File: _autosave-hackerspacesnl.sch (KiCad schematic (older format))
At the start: 55 parts, among them J1 Screw_Terminal_01x02, J2 Conn_01x04_Male, Q1 Q_NMOS_GSD, Q2 Q_NMOS_GSD, Q3 Q_NMOS_GSD, Q4 Q_NMOS_GSD, Q5 Q_NMOS_GSD, Q6 Q_NMOS_GSD, SW1 SW_Push, SW2 SW_Push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

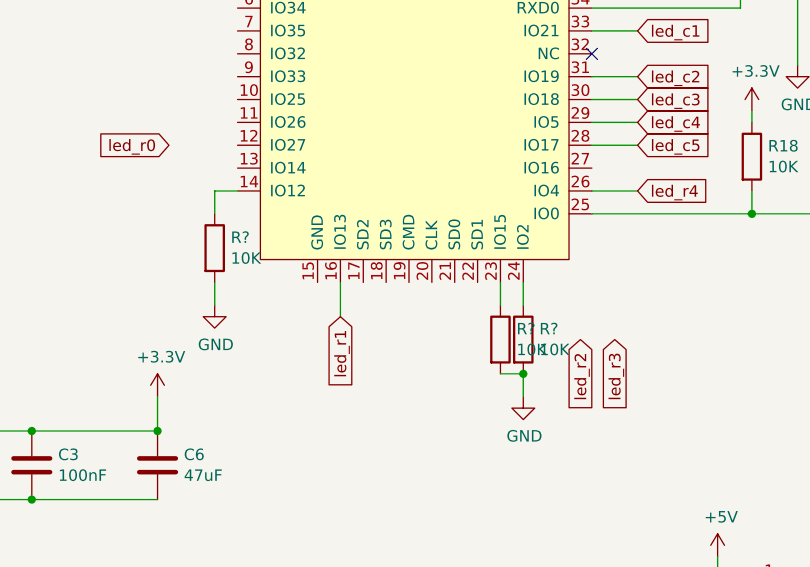
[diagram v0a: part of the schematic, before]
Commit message: bezig met nieuwe kaart, leds geplaatst en test van traces
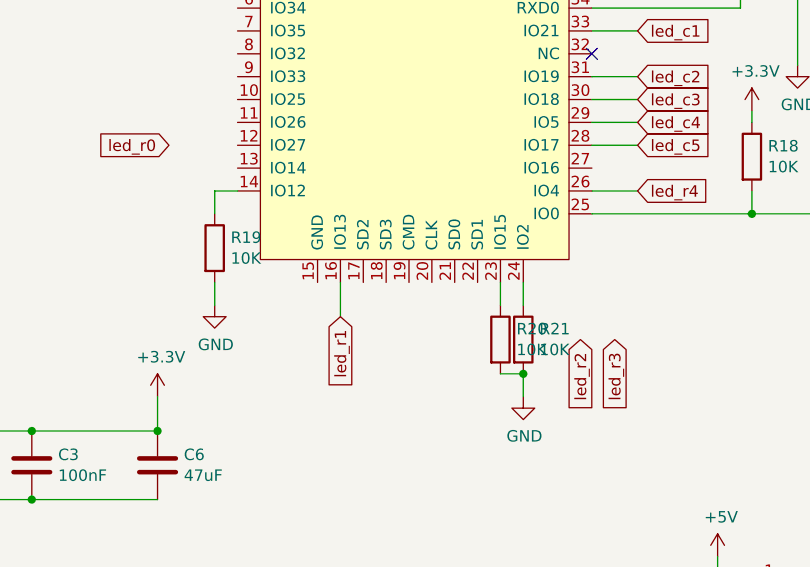
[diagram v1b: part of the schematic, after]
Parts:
- gave numbers to parts that had none: 3
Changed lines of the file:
@@
 led_r0
 $Comp
-L Device:R R?
+L Device:R R19
 U 1 1 5E08F19E
 P 7250 4100
-F 0 "R?" H 7320 4146 50  0000 L CNN
+F 0 "R19" H 7320 4146 50  0000 L CNN
 F 1 "10K" H 7320 4055 50  0000 L CNN
 F 2 "Resistor_SMD:R_0603_1608Metric" V 7180 4100 50  0001 C CNN
@@
 $EndComp
 $Comp
-L power:GND #PWR?
+L power:GND #PWR0101
 U 1 1 5E08FA41
 P 7250 4350
-F 0 "#PWR?" H 7250 4100 50  0001 C CNN
+F 0 "#PWR0101" H 7250 4100 50  0001 C CNN
 F 1 "GND" H 7255 4177 50  0000 C CNN
 F 2 "" H 7250 4350 50  0001 C CNN
@@
 	7250 3850 7350 3850
 $Comp
-L Device:R R?
+L Device:R R21
 U 1 1 5E0D9D1B
 P 8600 4500
-F 0 "R?" H 8670 4546 50  0000 L CNN
+F 0 "R21" H 8670 4546 50  0000 L CNN
 F 1 "10K" H 8670 4455 50  0000 L CNN
 F 2 "Resistor_SMD:R_0603_1608Metric" V 8530 4500 50  0001 C CNN
@@
 $EndComp
 $Comp
-L Device:R R?
+L Device:R R20
 U 1 1 5E0DA0FC
 P 8500 4500
-F 0 "R?" H 8570 4546 50  0000 L CNN
+F 0 "R20" H 8570 4546 50  0000 L CNN
 F 1 "10K" H 8570 4455 50  0000 L CNN
 F 2 "Resistor_SMD:R_0603_1608Metric" V 8430 4500 50  0001 C CNN
@@
 $EndComp
 $Comp
-L power:GND #PWR?
+L power:GND #PWR0102
 U 1 1 5E0DA27C
 P 8600 4750
-F 0 "#PWR?" H 8600 4500 50  0001 C CNN
+F 0 "#PWR0102" H 8600 4500 50  0001 C CNN
 F 1 "GND" H 8605 4577 50  0000 C CNN
 F 2 "" H 8600 4750 50  0001 C CNN
